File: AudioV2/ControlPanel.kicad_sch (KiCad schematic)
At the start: 39 parts, among them SW1 PWR SW, SW2 DEST sense (3PDT 3rd pole), U1 Pico 2 / RP2350, U2 PT2314-D, U5 BP5293-50 +5V

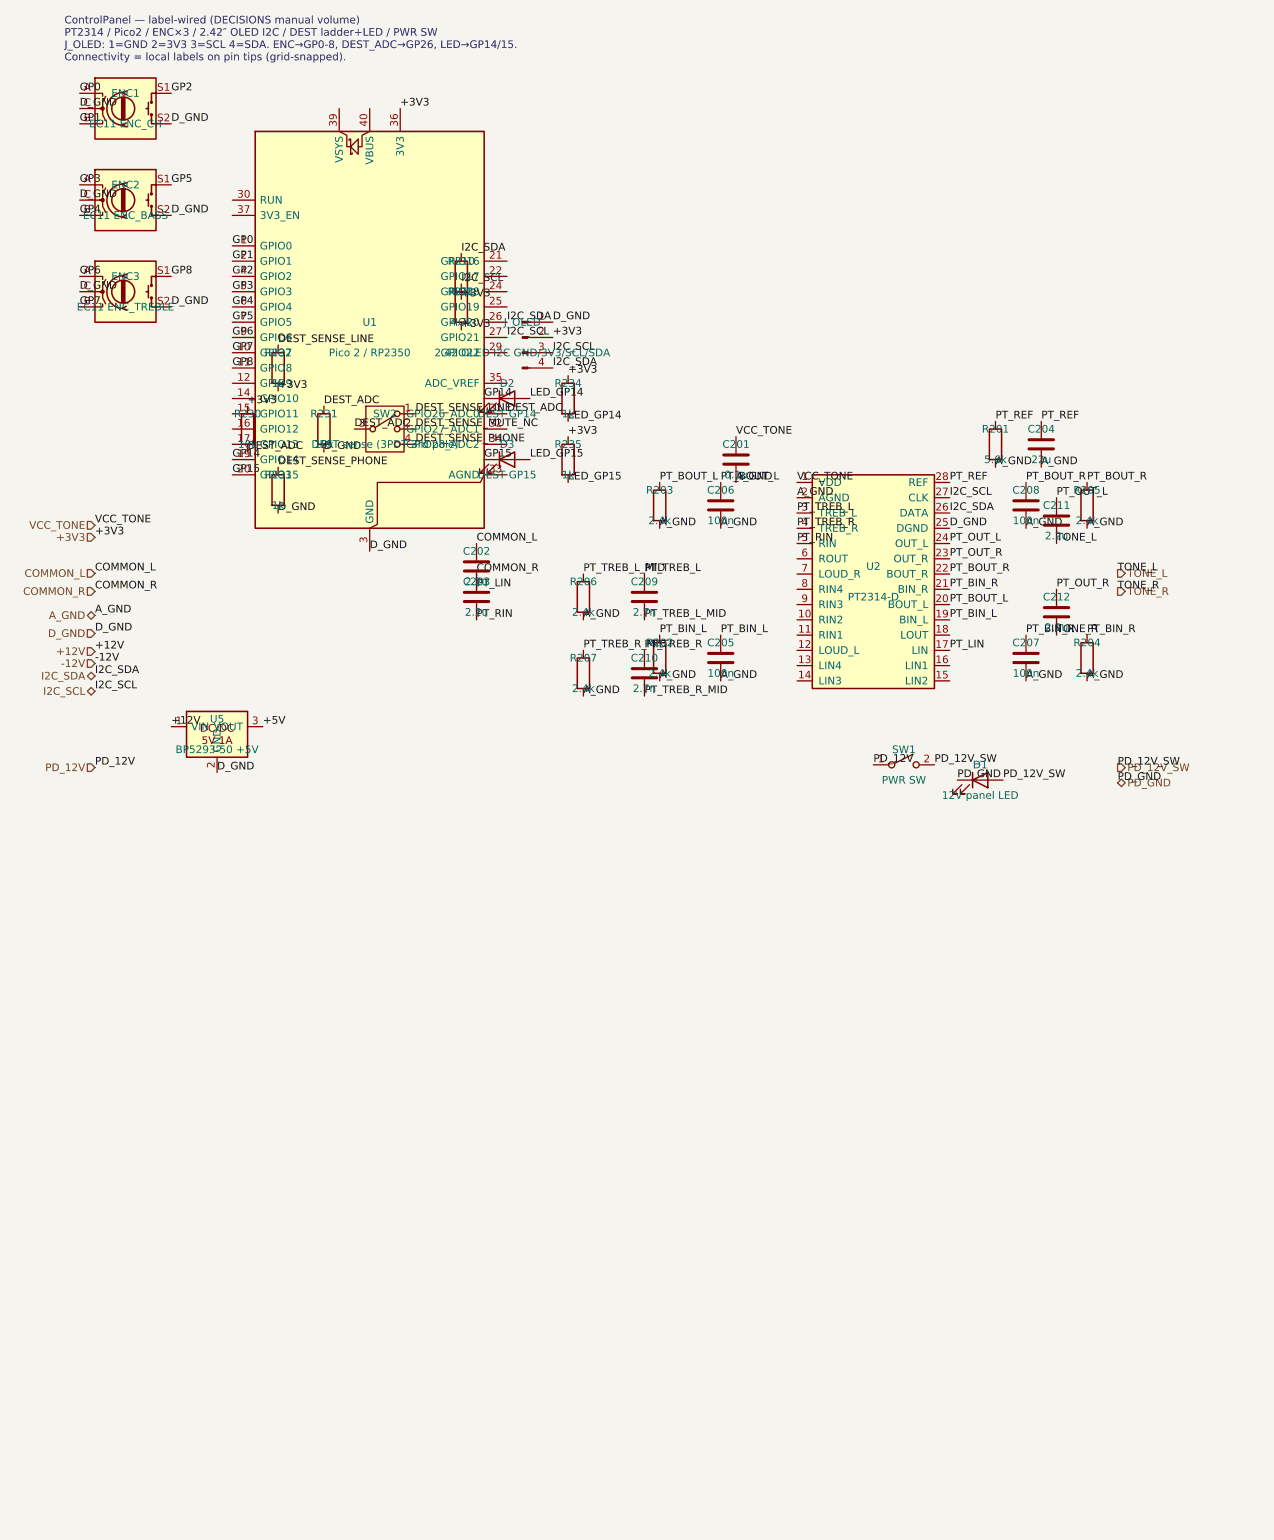
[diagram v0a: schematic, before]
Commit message: AudioV2: Power PD端子整理とエージェント引き継ぎ更新
PowerModule に J201/J202/J203 を揃え、PWR SW は ControlPanel に戻す。
AGENT_HANDOFF / WIRING に現状トポロジと PD A/B メモを残し、クラウド同期用に main へ載せる。

Co-authored-by: Cursor <cursoragent@cursor.com>
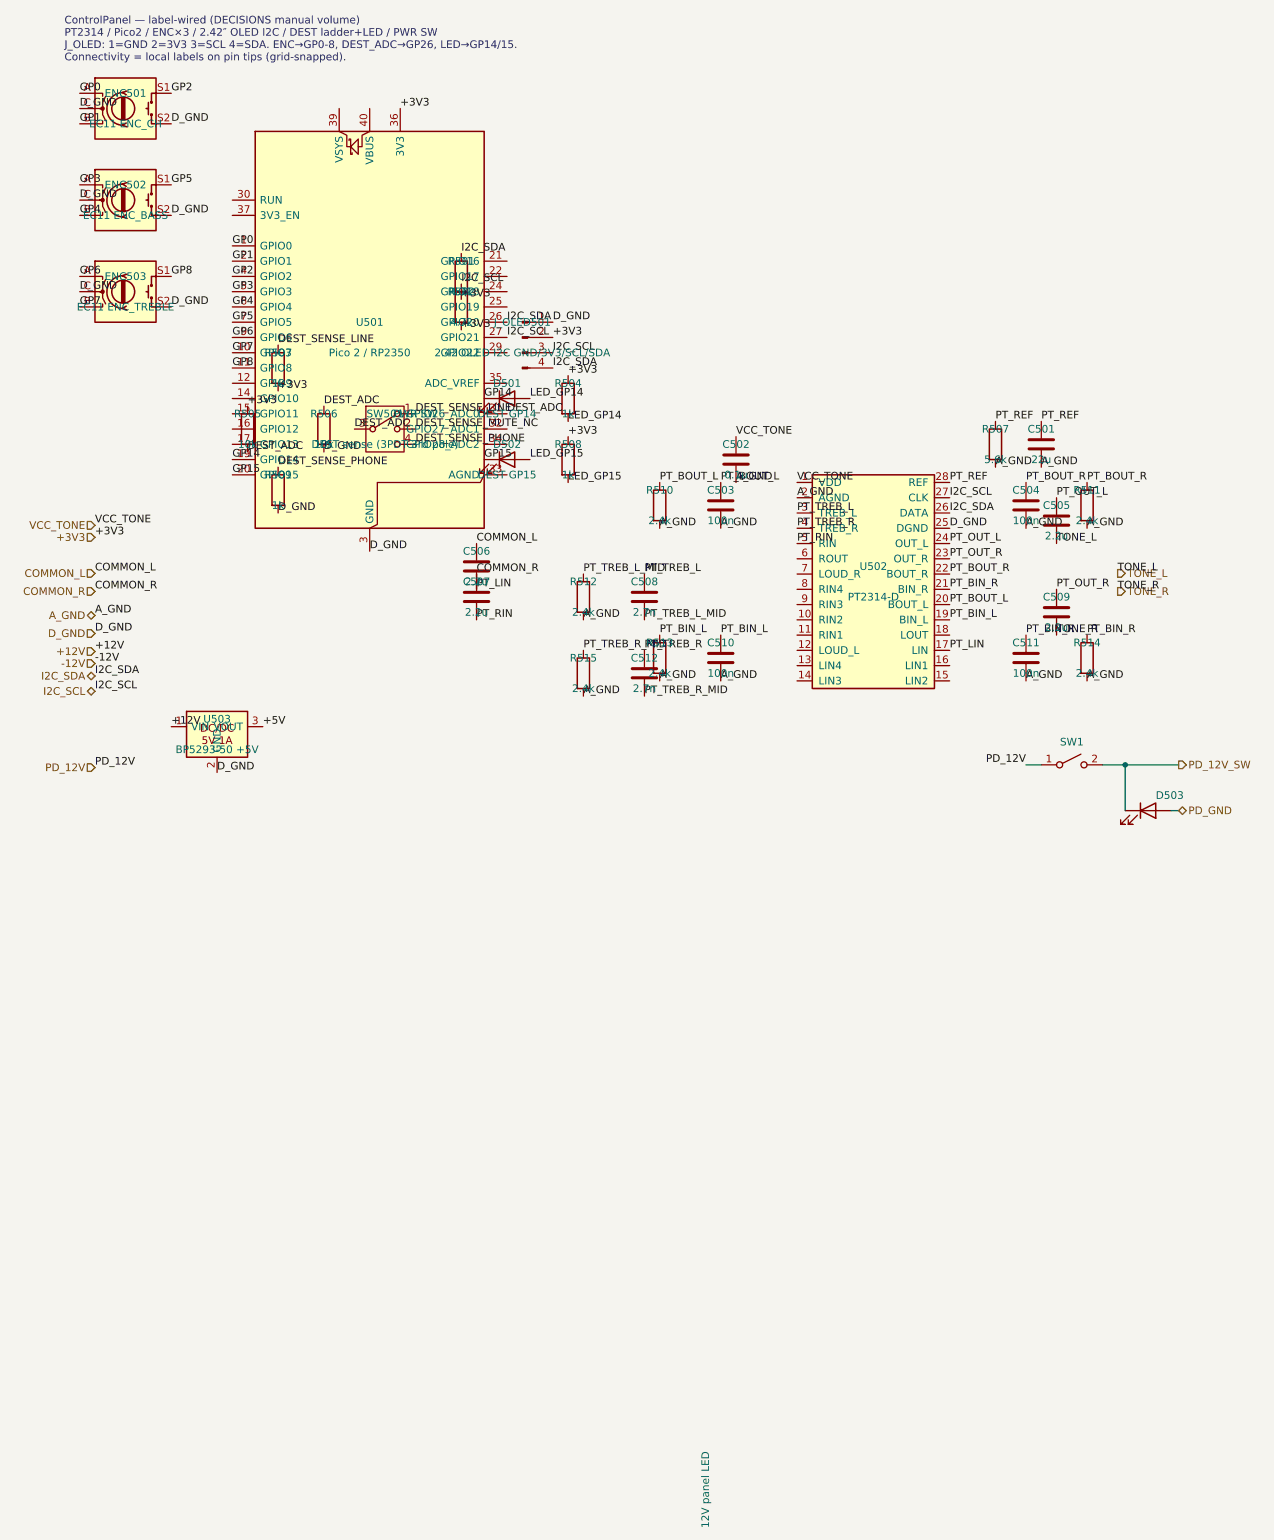
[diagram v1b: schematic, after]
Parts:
- removed D1: 12V panel LED, symbol Device:LED
- added D503: 12V panel LED, symbol Device:LED
- renumbered C204 to C501, C201 to C502, C206 to C503, C208 to C504, C211 to C505, C202 to C506, C203 to C507, C209 to C508, C212 to C509, C205 to C510, C207 to C511, C210 to C512, D2 to D501, D3 to D502, ENC1 to ENC501, ENC2 to ENC502, ENC3 to ENC503, J_OLED to J_OLED501, R210 to R501, R211 to R502, R232 to R503, R234 to R504, R230 to R505, R231 to R506, R201 to R507, R235 to R508, R233 to R509, R203 to R510, R205 to R511, R206 to R512, R202 to R513, R204 to R514, R207 to R515, SW2 to SW501, U1 to U501, U2 to U502, U5 to U503
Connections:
- net PD_12V_SW: now also D503.1 (K)
- net PD_GND: now also D503.2 (A)
